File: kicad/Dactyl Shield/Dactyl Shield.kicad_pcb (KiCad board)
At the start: 4 copper layers, 99.4 x 77.4 mm, 122 parts, among them J201 JST, J202 Split, J203 Column, J204 Thumb, J205 Foot, J206 Row, J207 Display, J208 Vic, J209 ResA, J212 ResB, J301 JST, J302 Split, J303 Column, J304 Thumb, J305 Foot, J306 Row, J307 Display, J308 Vic, J309 ResA, J312 ResB, Q201 AO3400A, Q301 AO3400A, SW201 Battery, SW202 Reset, SW203 LED, SW301 Battery, SW302 Reset, SW303 LED, U201 SRV05-4, U202 Nice!Nano/2040, U301 SRV05-4, U302 Nice!Nano/2040

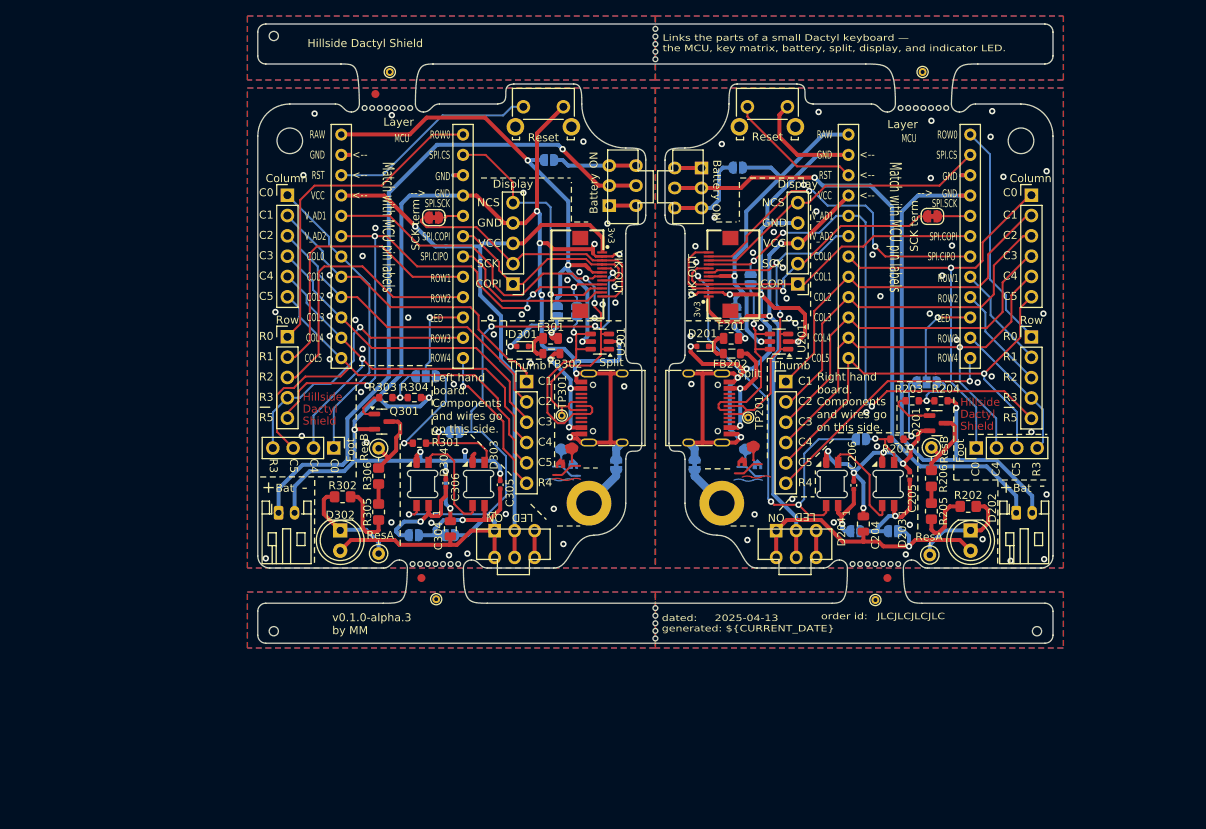
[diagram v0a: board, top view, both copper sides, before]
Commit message: feat: key headers match body grid layout (rough)
- Right hand only and just a rought sketch so far
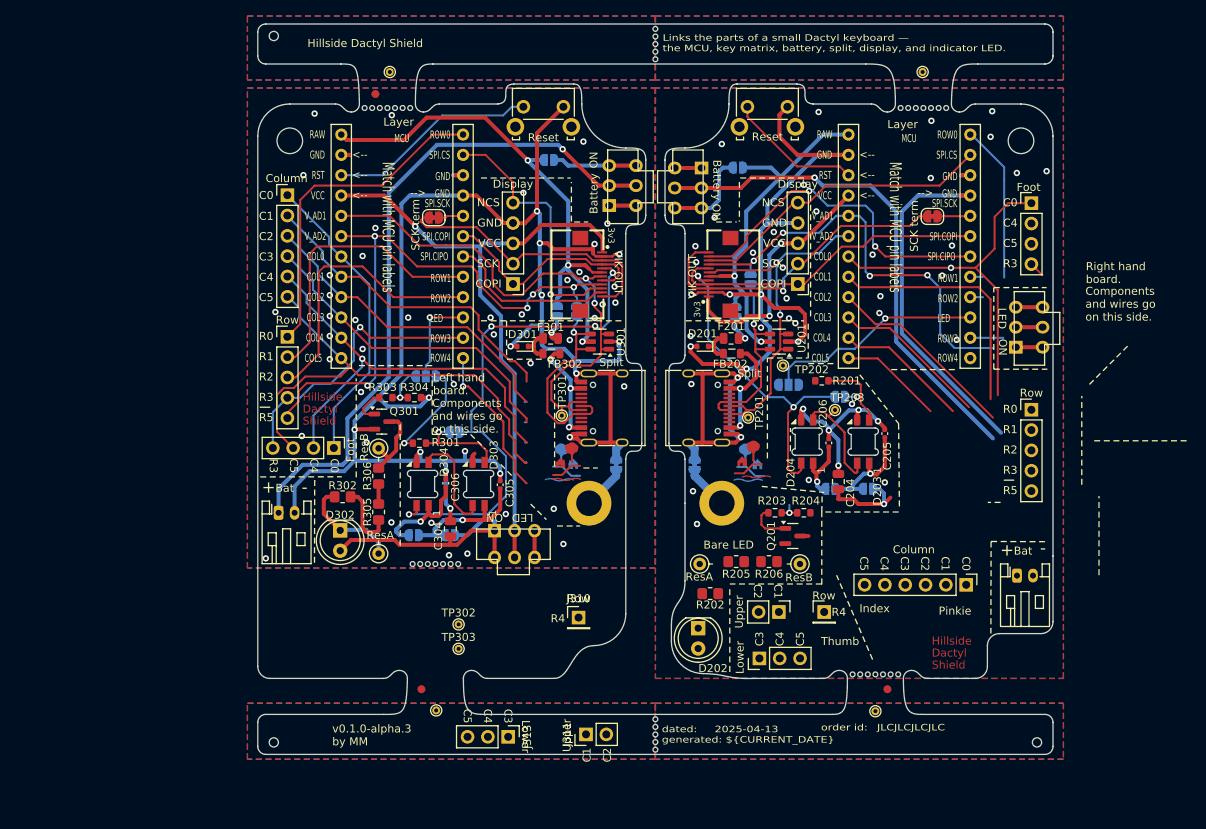
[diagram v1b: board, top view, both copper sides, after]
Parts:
- removed J204, J304: Thumb, Dactyl:PinHeader_Thumbs
- added J210: Thumb_row, Dactyl:PinHeader_Thumb_row, F.Cu at (160.6, 138.5)
- added J211: Thumb_upper, Dactyl:PinHeader_Thumb_upper, F.Cu at (154.9, 138.5)
- added J213: Thumb_lower, Dactyl:PinHeader_Thumb_lower, F.Cu at (152.5, 144.3)
- added J310: Thumb_row, Dactyl:PinHeader_Thumb_row, F.Cu at (129.9, 139.2)
- added J311: Thumb_upper, Dactyl:PinHeader_Thumb_upper, F.Cu at (130.8, 153.8)
- added J313: Thumb_lower, Dactyl:PinHeader_Thumb_lower, F.Cu at (121.1, 154.1)
- added TP202: TestPoint_Small, TestPoint:TestPoint_THTPad_D1.0mm_Drill0.5mm, F.Cu at (155.4, 107.7)
- added TP203: TestPoint_Small, TestPoint:TestPoint_THTPad_D1.0mm_Drill0.5mm, F.Cu at (161.9, 113.2)
- added TP302: TestPoint_Small, TestPoint:TestPoint_THTPad_D1.0mm_Drill0.5mm, F.Cu at (114.9, 140.1)
- added TP303: TestPoint_Small, TestPoint:TestPoint_THTPad_D1.0mm_Drill0.5mm, F.Cu at (114.9, 143.1)
- moved J203 49.4 mm to (178.3, 135.1), turned to -90 degrees
- moved SW203 39.8 mm to (186.2, 102.9), turned to 90 degrees
- moved D202 36.2 mm to (144.8, 140.5)
- moved R202 34.0 mm to (146.3, 136.2), turned to 180 degrees
- moved J205 31.4 mm to (186.5, 87.4), turned to 0 degrees
- moved REF** 30.1 mm to (176.8, 143.7)
- moved J209 28.8 mm to (145.0, 132.5), turned to 90 degrees
- moved R205 25.2 mm to (149.6, 132.2), turned to 180 degrees
- moved Q201 22.9 mm to (156.7, 129.0)
- moved R206 22.8 mm to (153.7, 132.2), turned to 180 degrees
- moved R203 22.1 mm to (154.4, 126.1)
- moved R204 22.1 mm to (158.1, 126.1)
- moved J212 22.0 mm to (157.6, 132.5), turned to -90 degrees
- moved JP208 17.3 mm to (156.2, 110.1), turned to 0 degrees
- moved FID102 13.9 mm to (110.2, 148.2)
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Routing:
- net /Right/col5: track 57.2 -> 13.0 mm, vias 1 -> 0
- net /Right/col4: track 59.8 -> 16.9 mm, vias 1 -> 0
- net /Right/GND: track 237.6 -> 203.3 mm, vias 59 -> 46
- net /Right/row4: track 31.2 -> 0.22 mm, vias 1 -> 0
- net /Right/VCC: track 60.0 -> 31.2 mm
- net /Right/col3: track 45.7 -> 19.7 mm
- net /Right/col2: track 45.9 -> 24.3 mm
- net /Right/VCC_LED: track 31.3 -> 11.2 mm
- net /Right/SPLIT-_R5: track 69.8 -> 53.8 mm, vias 3 -> 4
- net /Right/LED_out: track 56.3 -> 40.5 mm, vias 3 -> 2
- net /Right/LED: track 12.8 -> 28.4 mm
- net /Right/bat+: track 75.4 -> 60.0 mm
- net /Right/col1: track 45.2 -> 31.4 mm
- net /Right/VCC_LED1: track 13.0 -> 0.00 mm
- net /Right/row3: track 17.9 -> 6.11 mm
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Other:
- board size 99.4 x 77.4 mm -> 99.4 x 91.3 mm
- board text added: "Bare LED"
- board text added: "Index"
- board text added: "Pinkie"
- board text added: "Smart|Bare"
- board text added: "Thumb"
- board text removed: "Bare | Smart"

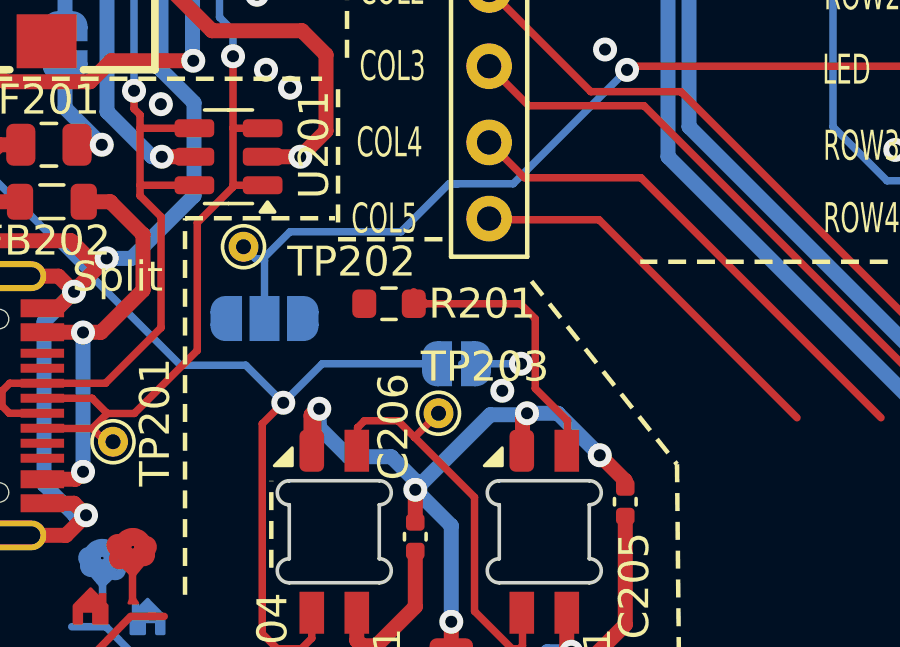
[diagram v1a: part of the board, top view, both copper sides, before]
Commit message: feat: move LED test point
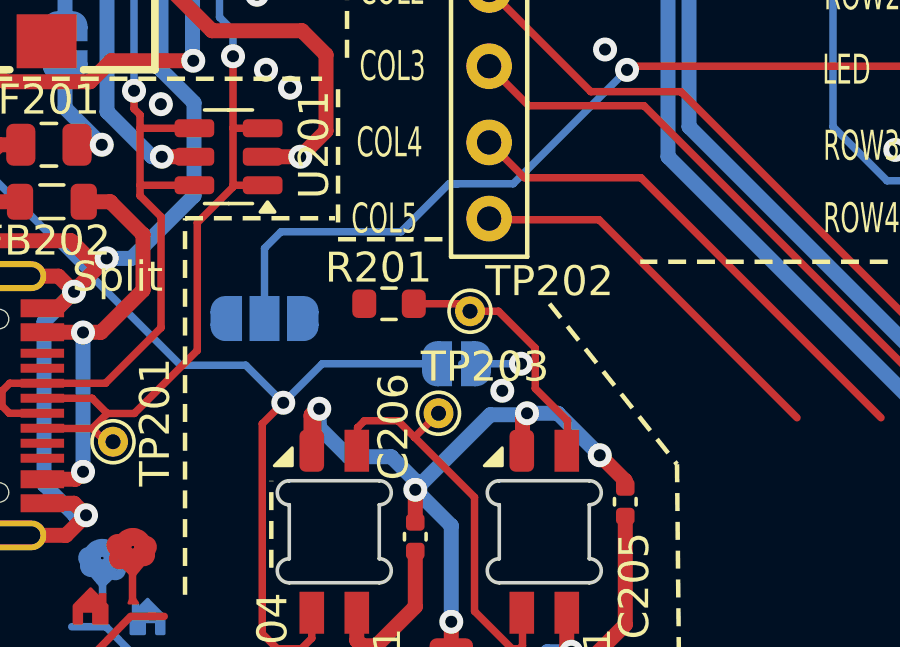
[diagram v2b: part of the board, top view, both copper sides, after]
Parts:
- moved TP202 7.85 mm to (163.0, 109.8)
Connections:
- TP202 pad 1: /Right/LED -> Net-(D203-DIN)
- TP302 pad 1: /Left/LED -> Net-(D303-DIN)
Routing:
- net Net-(D203-DIN): track 11.7 -> 10.6 mm
- net /Right/LED: track 28.4 -> 27.8 mm
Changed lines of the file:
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@@
 		(tags "resistor")
 		(property "Reference" "R201"
-			(at 3.1 0 0)
+			(at -0.35 -1.2 0)
 			(layer "F.SilkS")
 			(effects
@@
 			(layers "*.Cu" "*.Mask")
 			(remove_unused_layers no)
-			(net 66 "/Left/LED")
+			(net 41 "Net-(D303-DIN)")
 			(pinfunction "1")
 			(pintype "passive")
@@
 	(footprint "TestPoint:TestPoint_THTPad_D1.0mm_Drill0.5mm"
 		(layer "F.Cu")
-		(at 155.45 107.7)
+		(at 163 109.85)
 		(descr "THT pad as test Point, diameter 1.0mm, hole diameter 0.5mm")
 		(tags "test point THT pad")
 		(property "Reference" "TP202"
-			(at 3.6 0.5 0)
+			(at 2.65 -1 0)
 			(layer "F.SilkS")
 			(effects
@@
 			(layers "*.Cu" "*.Mask")
 			(remove_unused_layers no)
-			(net 1 "/Right/LED")
+			(net 32 "Net-(D203-DIN)")
 			(pinfunction "1")
 			(pintype "passive")
@@
 	)
 	(gr_line
-		(start 165.05 108.85)
+		(start 165.65 109.6)
 		(end 169.9 114.95)
 		(stroke
@@
 	)
 	(segment
-		(start 155.85 108.1)
-		(end 155.45 107.7)
-		(width 0.25)
-		(layer "B.Cu")
-		(net 1)
-	)
-	(segment
-		(start 156.15 109.8425)
-		(end 156.4 110.0925)
-		(width 0.25)
-		(layer "B.Cu")
-		(net 1)
-	)
-	(segment
-		(start 156.1 108.1)
-		(end 155.85 108.1)
-		(width 0.25)
-		(layer "B.Cu")
-		(net 1)
-	)
-	(segment
-		(start 162.6 105.6)
+		(start 160.7 107.2)
 		(end 162.3 105.6)
 		(width 0.25)
@@
 	)
 	(segment
-		(start 164.438242 105.6)
-		(end 168.232883 101.805359)
+		(start 156.15 107.75)
+		(end 156.7 107.2)
 		(width 0.25)
 		(layer "B.Cu")
@@
 	)
 	(segment
-		(start 156.15 108.15)
-		(end 156.15 109.8425)
+		(start 162.3 105.6)
+		(end 162.6 105.6)
 		(width 0.25)
 		(layer "B.Cu")
@@
 	)
 	(segment
-		(start 156.1 108.1)
-		(end 156.15 108.15)
+		(start 156.4 110.0925)
+		(end 156.15 109.8425)
 		(width 0.25)
 		(layer "B.Cu")
@@
 	)
 	(segment
-		(start 162.3 105.6)
+		(start 156.7 107.2)
 		(end 160.7 107.2)
 		(width 0.25)
@@
 	)
 	(segment
-		(start 162.5 105.6)
-		(end 164.438242 105.6)
+		(start 164.438242 105.6)
+		(end 168.232883 101.805359)
 		(width 0.25)
 		(layer "B.Cu")
@@
 	)
 	(segment
-		(start 160.7 107.2)
-		(end 157 107.2)
+		(start 156.15 109.8425)
+		(end 156.15 107.75)
 		(width 0.25)
 		(layer "B.Cu")
@@
 	)
 	(segment
-		(start 157 107.2)
-		(end 156.1 108.1)
+		(start 162.5 105.6)
+		(end 164.438242 105.6)
 		(width 0.25)
 		(layer "B.Cu")
@@
 	)
 	(segment
-		(start 165.175 111.6)
-		(end 165.175 110.1)
-		(width 0.25)
-		(layer "F.Cu")
-		(net 32)
-	)
-	(segment
-		(start 165.175 110.1)
-		(end 164.675 109.6)
+		(start 163.95 109.85)
+		(end 163 109.85)
 		(width 0.25)
 		(layer "F.Cu")
@@
 	)
 	(segment
-		(start 164.675 109.6)
-		(end 161.525 109.6)
+		(start 165.175 111.075)
+		(end 163.95 109.85)
 		(width 0.25)
 		(layer "F.Cu")
@@
 	(segment
 		(start 161.525 109.6)
-		(end 161.125 109.2)
+		(end 162.75 109.6)
+		(width 0.25)
+		(layer "F.Cu")
+		(net 32)
+	)
+	(segment
+		(start 165.175 111.6)
+		(end 165.175 111.075)
 		(width 0.25)
 		(layer "F.Cu")
@@
 		(width 0.25)
 		(layer "F.Cu")
+		(net 32)
+	)
+	(segment
+		(start 162.75 109.6)
+		(end 163 109.85)
+		(width 0.25)
+		(layer "F.Cu")

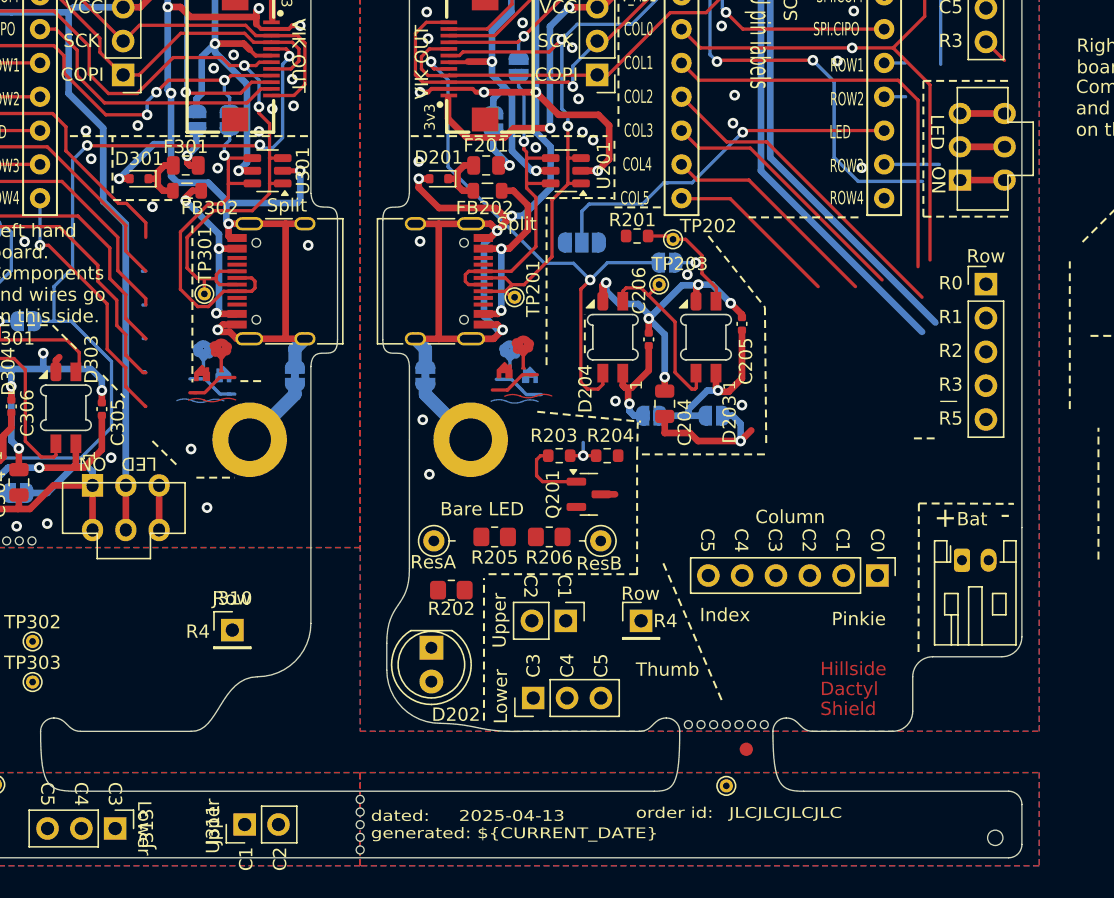
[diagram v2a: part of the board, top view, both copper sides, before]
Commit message: feat: move bare LED down a bit
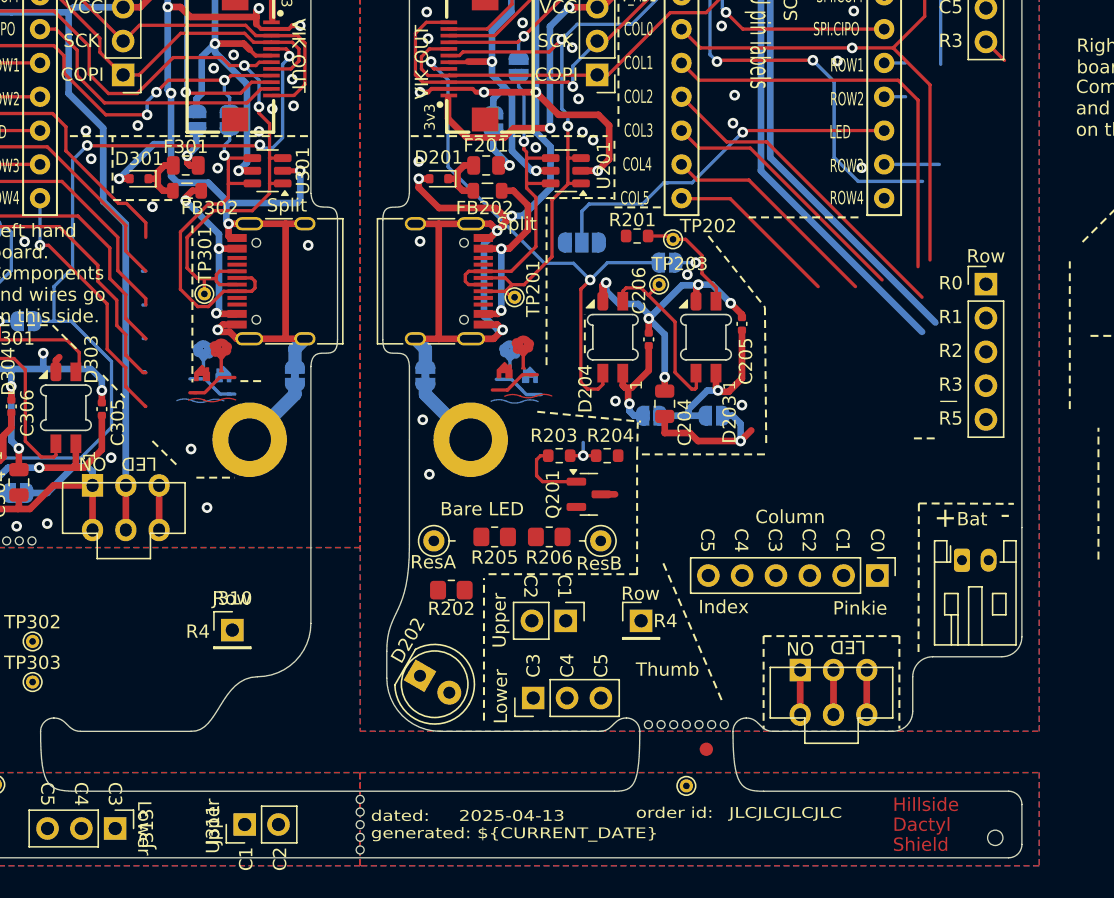
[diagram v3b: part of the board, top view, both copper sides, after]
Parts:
- moved SW203 42.5 mm to (175.1, 143.9), turned to 0 degrees
- moved REF** 11.6 mm to (182.2, 153.9)
- moved FID103 3.00 mm to (165.5, 148.2)
- moved REF** 3.00 mm to (164.0, 146.3)
- moved TP104 3.00 mm to (164.0, 150.9)
- moved D202 2.27 mm to (144.0, 142.6), turned to -30 degrees
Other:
- outline, holes or cut-outs redrawn
